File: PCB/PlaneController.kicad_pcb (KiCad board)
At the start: 2 copper layers, 45.7 x 86.4 mm, 14 parts, among them J1 Conn_01x06_Pin, J2 Conn_01x04_Pin, J3 Conn_01x03, J4 Conn_02x04_Odd_Even, M1 Motor_Servo, M2 Motor_Servo, M3 Motor_Servo, M4 Motor_Servo, M5 Motor_Servo

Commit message: Major PCB fix
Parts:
- J4: moved to B.Cu
- moved J4 2.55 mm to (96.8, 33.0), turned to -90 degrees
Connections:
- net /GDO1 renamed /GDO1 / GDO0
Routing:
- net Net-(A1-SCL/A5): track 91.0 -> 38.1 mm
- net /SCK: track 133.5 -> 107.3 mm
- net Net-(A1-RX1): track 83.7 -> 60.6 mm
- net /GDO1 / GDO0: track 105.8 -> 85.7 mm
- net Net-(A1-+5V): track 131.7 -> 112.7 mm
- net /3.3V: track 117.6 -> 136.1 mm
- net /GND: track 155.4 -> 137.6 mm
- net /GDO2: track 102.6 -> 90.2 mm
- net /MOSI: track 96.9 -> 90.0 mm, vias 0 -> 1
- net Net-(A1-SDA/A4): track 43.1 -> 45.3 mm
- net Net-(A1-D7): track 28.4 -> 30.2 mm
- net /MISO: track 111.0 -> 109.4 mm
- net /CSN: track 90.6 -> 89.8 mm
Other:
- board text added: "Arduino NANO"

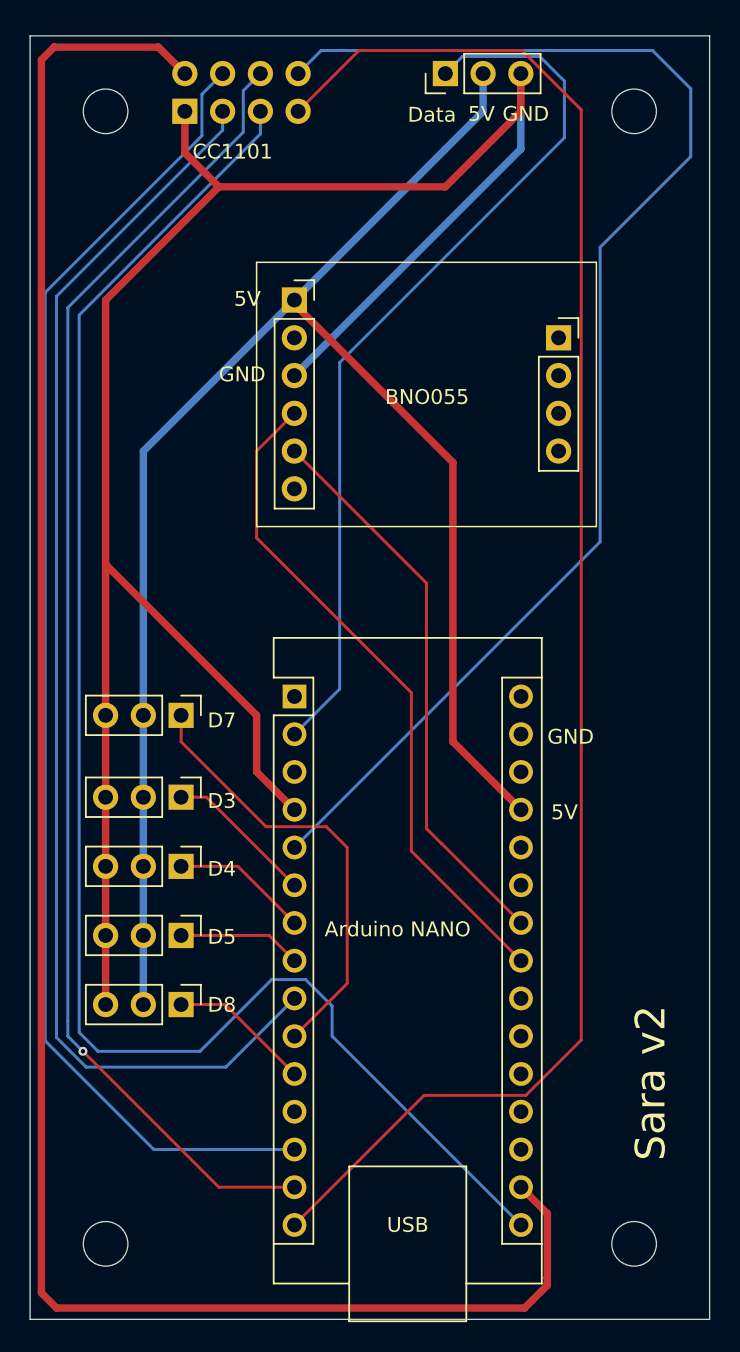
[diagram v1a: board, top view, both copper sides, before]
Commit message: Radio is now connected and unnecessary connections are removed from the pcb
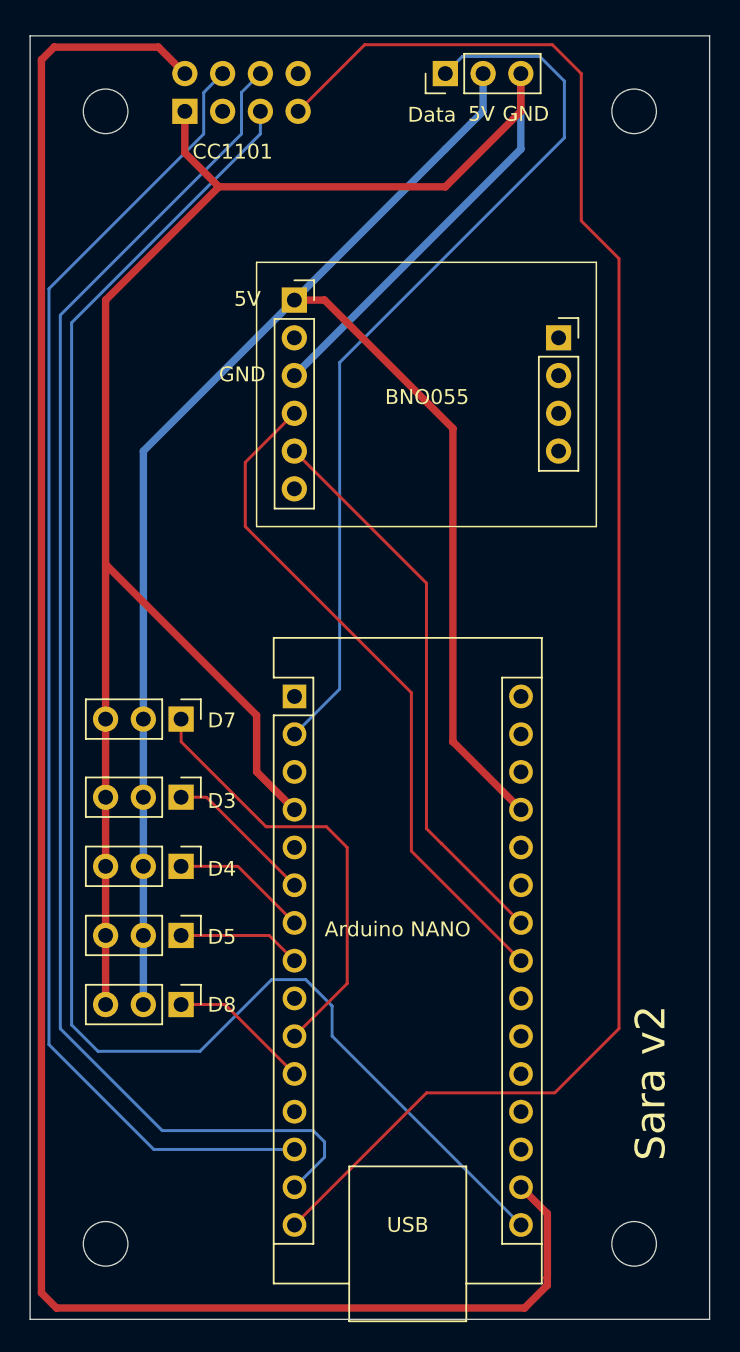
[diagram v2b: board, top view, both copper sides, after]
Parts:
- moved M1 0.25 mm to (96.5, 73.9)
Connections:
- A1 pad 5: /GDO2 -> unconnected-(A1-D2-Pad5)
- A1 pad 9: /GDO1 / GDO0 -> unconnected-(A1-D6-Pad9)
- J4 pad 3: /GDO1 / GDO0 -> /GD01
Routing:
- net /GDO2: track 90.2 -> 0.00 mm
- net /GDO1 / GDO0: track 85.7 -> 0.00 mm
- net /MOSI: track 90.0 -> 95.0 mm, vias 1 -> 0
- net /MISO: track 109.4 -> 114.3 mm
- net Net-(A1-+5V): track 112.7 -> 113.9 mm
- net Net-(A1-SDA/A4): track 45.3 -> 45.9 mm

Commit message: Add 3 more GPIO pins to the main PCB
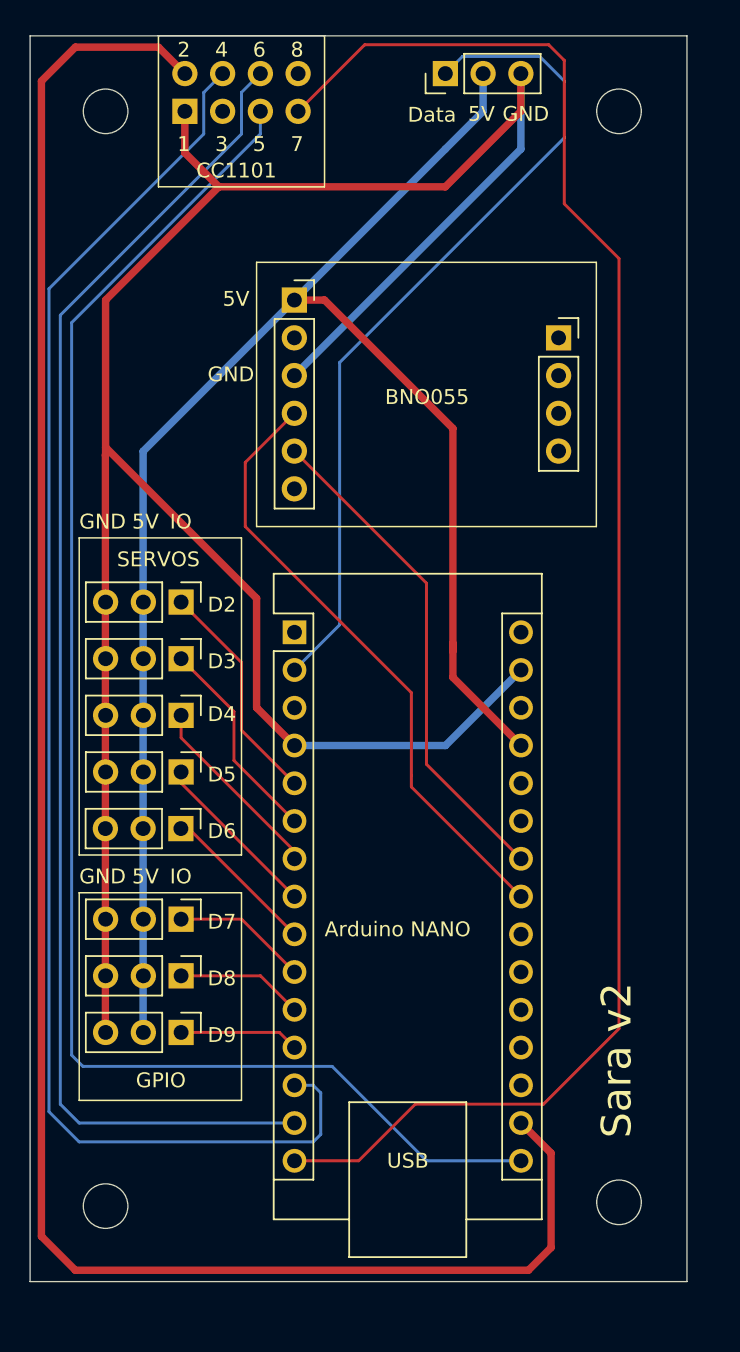
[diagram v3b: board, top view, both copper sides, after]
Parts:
- added J5: GPIO7, Connector_PinHeader_2.54mm:PinHeader_1x03_P2.54mm_Vertical, F.Cu at (96.5, 87.4)
- added J6: GPIO8, Connector_PinHeader_2.54mm:PinHeader_1x03_P2.54mm_Vertical, F.Cu at (96.5, 91.2)
- added J7: GPIO9, Connector_PinHeader_2.54mm:PinHeader_1x03_P2.54mm_Vertical, F.Cu at (96.5, 95.0)
- moved M5 11.8 mm to (96.5, 81.3)
- moved M4 11.0 mm to (96.5, 77.5)
- moved M3 10.2 mm to (96.5, 73.7)
- moved M2 9.32 mm to (96.5, 69.8)
- moved M1 7.87 mm to (96.5, 66.0)
- moved A1 4.32 mm to (104.2, 68.1)
- moved H4 2.97 mm to (126.0, 106.4)
- moved H3 2.54 mm to (91.4, 106.7)
- moved H1 1.02 mm to (126.0, 33.0)
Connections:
- A1 pad 12: unconnected-(A1-D9-Pad12) -> Net-(A1-D9)
- A1 pad 5: unconnected-(A1-D2-Pad5) -> Net-(A1-D2)
- A1 pad 9: unconnected-(A1-D6-Pad9) -> Net-(A1-D6)
- M1 pad 1: Net-(A1-D7) -> Net-(A1-D2)
- M5 pad 1: Net-(A1-D8) -> Net-(A1-D6)
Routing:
- net /GND: track 137.6 -> 160.4 mm
- net Net-(A1-D7): track 29.9 -> 9.35 mm
- net Net-(A1-D2): track 0.00 -> 15.4 mm
- net Net-(A1-D6): track 0.00 -> 10.6 mm
- net /CSN: track 89.6 -> 98.8 mm
- net Net-(A1-D9): track 0.00 -> 8.05 mm
- net /SCK: track 107.7 -> 101.9 mm
- net Net-(A1-SCL/A5): track 38.1 -> 33.7 mm
- net Net-(A1-RX1): track 60.6 -> 56.3 mm
- net Net-(A1-SDA/A4): track 45.9 -> 41.6 mm
- net Net-(A1-D3): track 10.1 -> 14.3 mm
- net Net-(A1-D4): track 9.21 -> 12.8 mm
- net /MOSI: track 95.0 -> 91.6 mm
- net Net-(A1-D5): track 8.33 -> 11.5 mm
- net /3.3V: track 136.1 -> 134.1 mm
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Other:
- board size 45.7 x 86.4 mm -> 44.2 x 83.8 mm
- board text added: "1"
- board text added: "2"
- board text added: "3"
- board text added: "4"
- board text added: "5"
- board text added: "6"
- board text added: "7"
- board text added: "8"
- board text added: "D2"
- board text added: "D6"
- board text added: "D9"
- board text added: "GPIO"
- board text added: "IO"
- board text added: "SERVOS"

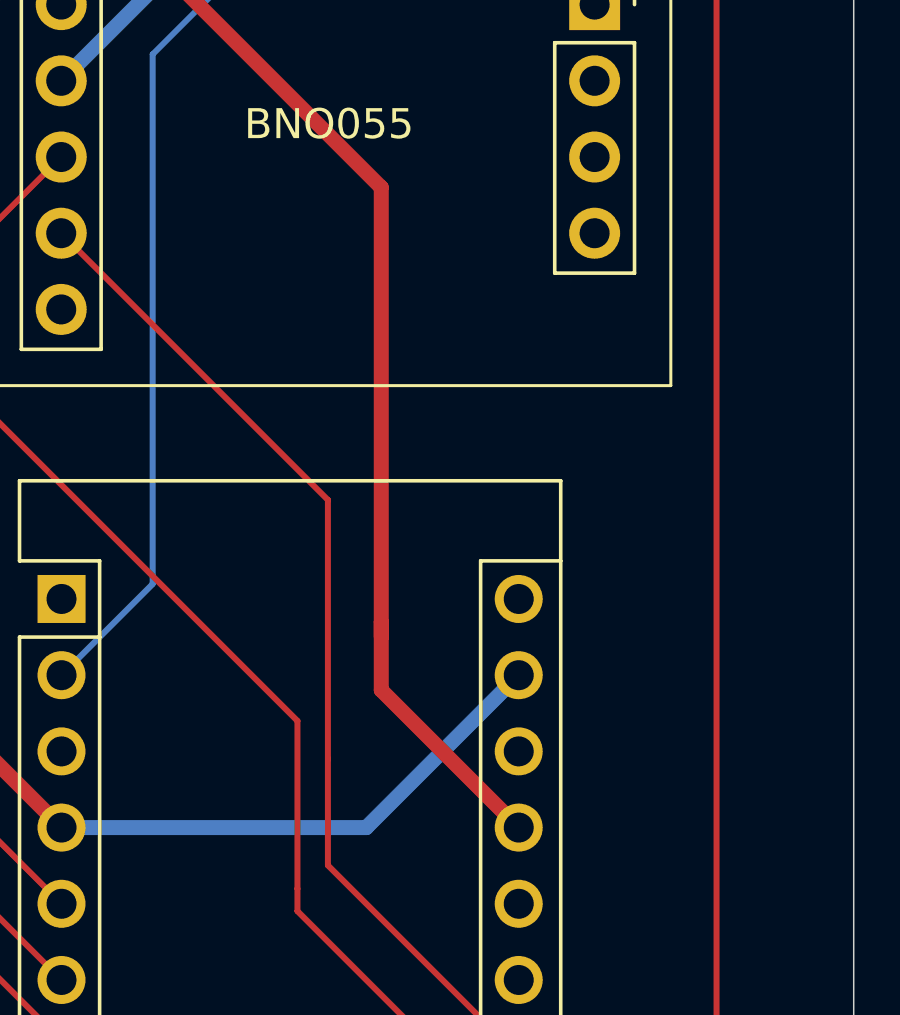
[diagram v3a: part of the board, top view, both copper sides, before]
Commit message: Add ground station code
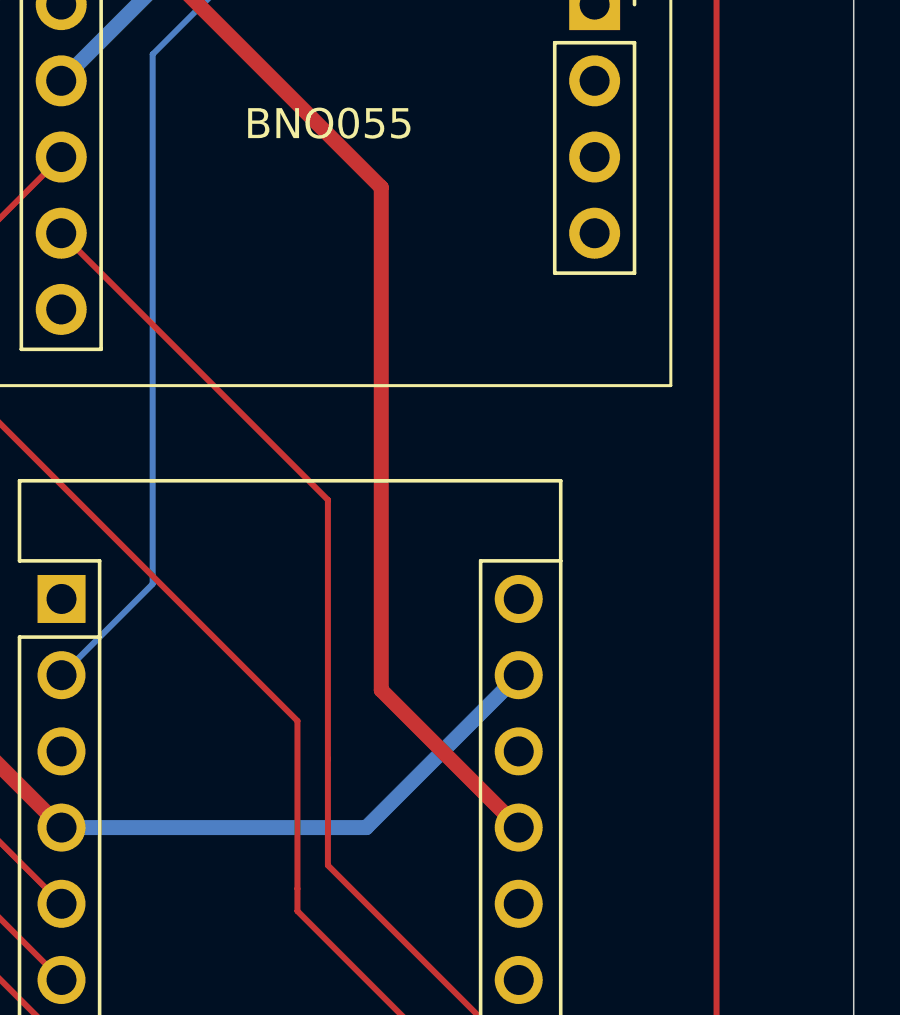
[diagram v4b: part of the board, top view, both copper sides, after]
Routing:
- net Net-(A1-+5V): track 113.8 -> 111.5 mm
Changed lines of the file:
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@@
-	)
-	(segment
-		(start 119.39 75.692)
-		(end 114.808 71.11)
-		(width 0.5)
-		(layer "F.Cu")
-		(net 7)
-	)
-	(segment
-		(start 114.808 71.11)
-		(end 114.808 68.834)
-		(width 0.5)
-		(layer "F.Cu")
-		(net 7)
-	)
-	(segment
-		(start 114.808 54.356)
-		(end 114.808 68.834)
-		(width 0.5)
-		(layer "F.Cu")
-		(net 7)
-	)
-	(segment
-		(start 114.808 68.834)
-		(end 114.808 69.342)
-		(width 0.5)
-		(layer "F.Cu")
-		(net 7)
 	)
 	(segment
@@
 	(segment
 		(start 114.808 71.11)
-		(end 114.808 69.342)
-		(width 0.2)
+		(end 119.39 75.692)
+		(width 0.5)
 		(layer "F.Cu")
 		(net 7)
+	)
+	(segment
+		(start 114.808 54.356)
+		(end 114.808 71.11)
+		(width 0.5)
+		(layer "F.Cu")
+		(net 7)
